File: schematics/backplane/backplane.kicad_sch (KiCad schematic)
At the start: 9 parts

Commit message: Update backplane, add power supply and debug port
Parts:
- removed MOD9: Module, cpu816footprints:BusSlot, symbol cpu816symbols:BusSlot
- added J1: Conn_01x02, Connector_BarrelJack:BarrelJack_SwitchcraftConxall_RAPC10U_Horizontal, symbol Connector_Generic:Conn_01x02
- added J2: Conn_01x20, Connector_PinSocket_2.54mm:PinSocket_1x20_P2.54mm_Vertical, symbol Connector_Generic:Conn_01x20
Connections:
- net DATA0: now also J2.13 (Pin_13)
- net DATA1: now also J2.14 (Pin_14)
- net DATA2: now also J2.15 (Pin_15)
- net DATA3: now also J2.16 (Pin_16)
- net DATA4: now also J2.17 (Pin_17)
- net DATA5: now also J2.18 (Pin_18)
- net DATA6: now also J2.19 (Pin_19)
- net DATA7: now also J2.20 (Pin_20)
- net GND: now also J1.2 (Pin_2), J2.1 (Pin_1), J2.2 (Pin_2)
- net PCINC: now also J2.4 (Pin_4)
- net STATE10: now also J2.7 (Pin_7)
- net STATE11: now also J2.8 (Pin_8)
- net STATE12: now also J2.9 (Pin_9)
- net STATE13: now also J2.10 (Pin_10)
- net STATE14: now also J2.11 (Pin_11)
- net STATE15: now also J2.12 (Pin_12)
- net STATE8: now also J2.5 (Pin_5)
- net STATE9: now also J2.6 (Pin_6)
- net VCC: now also J1.1 (Pin_1)
- net ~{SCCLR}: now also J2.3 (Pin_3)

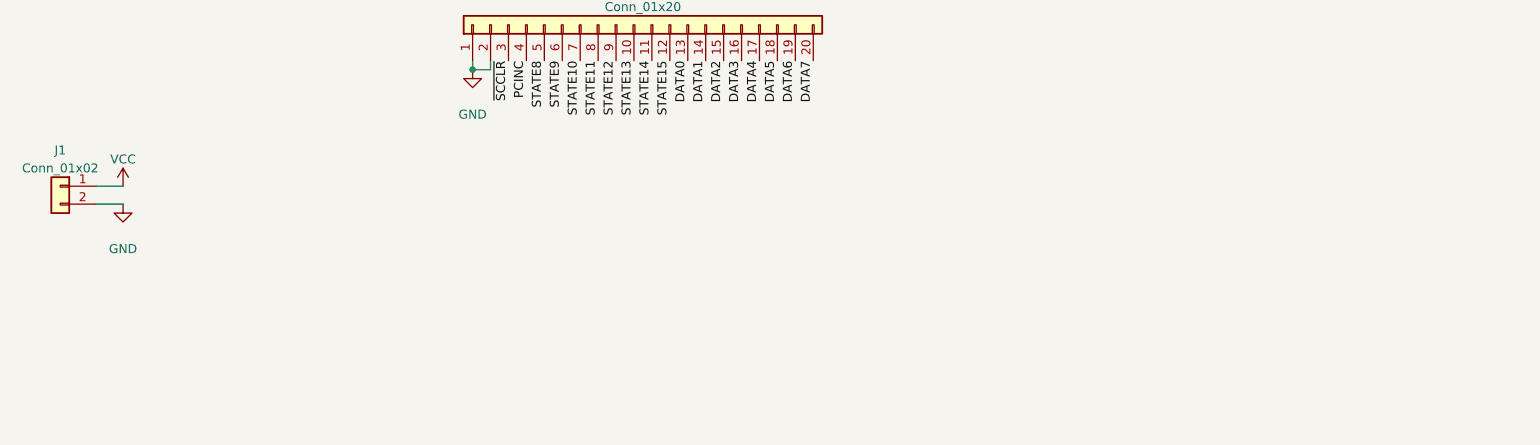
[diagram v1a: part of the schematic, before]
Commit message: fix(backplane): changed vcc and gnd connector
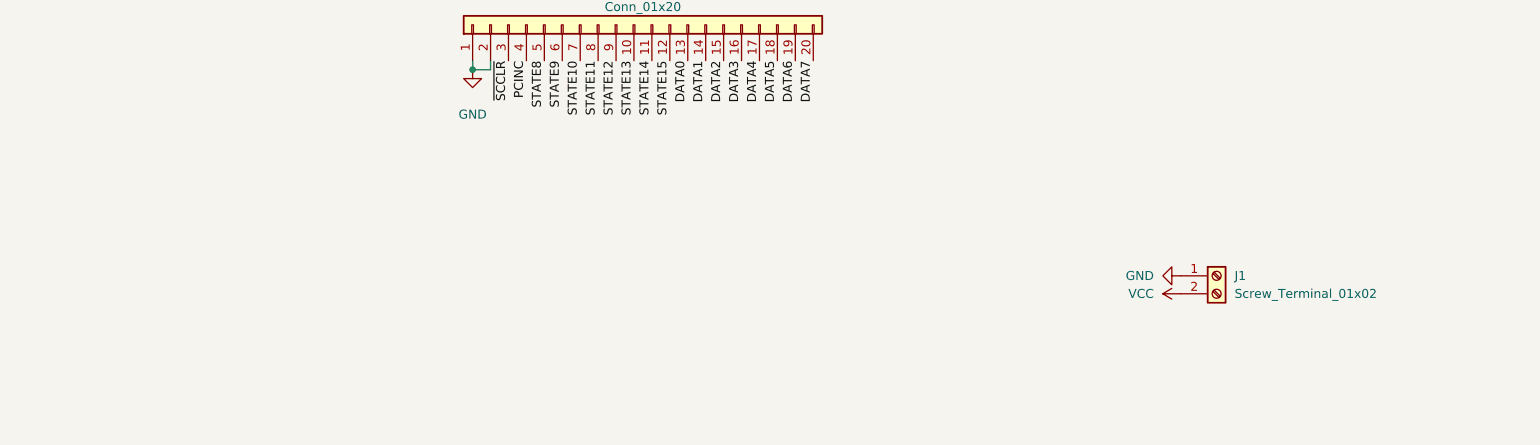
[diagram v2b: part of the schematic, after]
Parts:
- removed J1: Conn_01x02, Connector_BarrelJack:BarrelJack_SwitchcraftConxall_RAPC10U_Horizontal, symbol Connector_Generic:Conn_01x02
- added J1: Screw_Terminal_01x02, TerminalBlock_Phoenix:TerminalBlock_Phoenix_MKDS-1,5-2-5.08_1x02_P5.08mm_Horizontal, symbol Connector:Screw_Terminal_01x02
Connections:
- net GND: now also J1.1 (Pin_1)
- net VCC: now also J1.2 (Pin_2)
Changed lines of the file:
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@@
 	(wire
 		(pts
-			(xy -5.08 -12.7) (xy -8.89 -12.7)
-		)
-		(stroke
-			(width 0)
-			(type default)
-		)
-	)
-	(wire
-		(pts
-			(xy -5.08 -15.24) (xy -8.89 -15.24)
-		)
-		(stroke
-			(width 0)
-			(type default)
-		)
-	)
-	(wire
-		(pts
 			(xy 44.45 -33.02) (xy 44.45 -31.75)
 		)
@@
 	)
 	(symbol
-		(lib_id "power:VCC")
-		(at -5.08 -15.24 0)
-		(unit 1)
-		(exclude_from_sim no)
-		(in_bom yes)
-		(on_board yes)
-		(dnp no)
-		(property "Reference" "#PWR019"
-			(at -5.08 -11.43 0)
-			(effects
-				(font
-					(size 1.27 1.27)
-				)
-				(hide yes)
-			)
-		)
-		(property "Value" "VCC"
-			(at -5.08 -19.05 0)
-			(effects
-				(font
-					(size 1.27 1.27)
-				)
-			)
-		)
-		(property "Footprint" ""
-			(at -5.08 -15.24 0)
-			(effects
-				(font
-					(size 1.27 1.27)
-				)
-				(hide yes)
-			)
-		)
-		(property "Datasheet" ""
-			(at -5.08 -15.24 0)
-			(effects
-				(font
-					(size 1.27 1.27)
-				)
-				(hide yes)
-			)
-		)
-		(property "Description" "Power symbol creates a global label with name \"VCC\""
-			(at -5.08 -15.24 0)
-			(effects
-				(font
-					(size 1.27 1.27)
-				)
-				(hide yes)
-			)
-		)
-		(pin "1"
-		)
-		(instances
-			(project ""
-				(path "/805c276d-2b31-41a7-94f3-96d73c57e604"
-					(reference "#PWR019")
-					(unit 1)
-				)
-			)
-		)
-	)
-	(symbol
 		(lib_id "power:GND")
 		(at 466.09 165.1 0)
@@
 	)
 	(symbol
+		(lib_id "power:GND")
+		(at 144.78 -2.54 270)
+		(unit 1)
+		(exclude_from_sim no)
+		(in_bom yes)
+		(on_board yes)
+		(dnp no)
+		(fields_autoplaced yes)
+		(property "Reference" "#PWR019"
+			(at 138.43 -2.54 0)
+			(effects
+				(font
+					(size 1.27 1.27)
+				)
+				(hide yes)
+			)
+		)
+		(property "Value" "GND"
+			(at 140.97 -2.5401 90)
+			(effects
+				(font
+					(size 1.27 1.27)
+				)
+				(justify right)
+			)
+		)
+		(property "Footprint" ""
+			(at 144.78 -2.54 0)
+			(effects
+				(font
+					(size 1.27 1.27)
+				)
+				(hide yes)
+			)
+		)
+		(property "Datasheet" ""
+			(at 144.78 -2.54 0)
+			(effects
+				(font
+					(size 1.27 1.27)
+				)
+				(hide yes)
+			)
+		)
+		(property "Description" "Power symbol creates a global label with name \"GND\" , ground"
+			(at 144.78 -2.54 0)
+			(effects
+				(font
+					(size 1.27 1.27)
+				)
+				(hide yes)
+			)
+		)
+		(pin "1"
+		)
+		(instances
+			(project ""
+				(path "/805c276d-2b31-41a7-94f3-96d73c57e604"
+					(reference "#PWR019")
+					(unit 1)
+				)
+			)
+		)
+	)
+	(symbol
 		(lib_id "power:VCC")
 		(at 279.4 29.21 0)
@@
 	)
 	(symbol
-		(lib_id "power:GND")
-		(at -5.08 -12.7 0)
-		(unit 1)
-		(exclude_from_sim no)
-		(in_bom yes)
-		(on_board yes)
-		(dnp no)
-		(fields_autoplaced yes)
-		(property "Reference" "#PWR020"
-			(at -5.08 -6.35 0)
-			(effects
-				(font
-					(size 1.27 1.27)
-				)
-				(hide yes)
-			)
-		)
-		(property "Value" "GND"
-			(at -5.08 -6.35 0)
-			(effects
-				(font
-					(size 1.27 1.27)
-				)
-			)
-		)
-		(property "Footprint" ""
-			(at -5.08 -12.7 0)
-			(effects
-				(font
-					(size 1.27 1.27)
-				)
-				(hide yes)
-			)
-		)
-		(property "Datasheet" ""
-			(at -5.08 -12.7 0)
-			(effects
-				(font
-					(size 1.27 1.27)
-				)
-				(hide yes)
-			)
-		)
-		(property "Description" "Power symbol creates a global label with name \"GND\" , ground"
-			(at -5.08 -12.7 0)
-			(effects
-				(font
-					(size 1.27 1.27)
-				)
-				(hide yes)
-			)
-		)
-		(pin "1"
-		)
-		(instances
-			(project ""
-				(path "/805c276d-2b31-41a7-94f3-96d73c57e604"
-					(reference "#PWR020")
-					(unit 1)
-				)
-			)
-		)
-	)
-	(symbol
 		(lib_id "Connector_Generic:Conn_01x20")
 		(at 67.31 -38.1 90)
@@
 	)
 	(symbol
-		(lib_id "Connector_Generic:Conn_01x02")
-		(at -13.97 -15.24 0)
-		(mirror y)
-		(unit 1)
-		(exclude_from_sim no)
-		(in_bom yes)
-		(on_board yes)
-		(dnp no)
-		(fields_autoplaced yes)
-		(property "Reference" "J1"
-			(at -13.97 -20.32 0)
-			(effects
-				(font
-					(size 1.27 1.27)
-				)
-			)
-		)
-		(property "Value" "Conn_01x02"
-			(at -13.97 -17.78 0)
-			(effects
-				(font
-					(size 1.27 1.27)
-				)
-			)
-		)
-		(property "Footprint" "Connector_BarrelJack:BarrelJack_SwitchcraftConxall_RAPC10U_Horizontal"
-			(at -13.97 -15.24 0)
-			(effects
-				(font
-					(size 1.27 1.27)
-				)
-				(hide yes)
-			)
-		)
-		(property "Datasheet" "~"
-			(at -13.97 -15.24 0)
-			(effects
-				(font
-					(size 1.27 1.27)
-				)
-				(hide yes)
-			)
-		)
-		(property "Description" "Generic connector, single row, 01x02, script generated (kicad-library-utils/schlib/autogen/connector/)"
-			(at -13.97 -15.24 0)
-			(effects
-				(font
-					(size 1.27 1.27)
-				)
-				(hide yes)
-			)
-		)
-		(pin "2"
-		)
-		(pin "1"
-		)
-		(instances
-			(project ""
-				(path "/805c276d-2b31-41a7-94f3-96d73c57e604"
-					(reference "J1")
-					(unit 1)
-				)
-			)
-		)
-	)
-	(symbol
 		(lib_id "power:VCC")
 		(at 466.09 27.94 0)
@@
 	)
 	(symbol
+		(lib_id "Connector:Screw_Terminal_01x02")
+		(at 149.86 -2.54 0)
+		(unit 1)
+		(exclude_from_sim no)
+		(in_bom yes)
+		(on_board yes)
+		(dnp no)
+		(fields_autoplaced yes)
+		(property "Reference" "J1"
+			(at 152.4 -2.5401 0)
+			(effects
+				(font
+					(size 1.27 1.27)
+				)
+				(justify left)
+			)
+		)
+		(property "Value" "Screw_Terminal_01x02"
+			(at 152.4 -0.0001 0)
+			(effects
+				(font
+					(size 1.27 1.27)
+				)
+				(justify left)
+			)
+		)
+		(property "Footprint" "TerminalBlock_Phoenix:TerminalBlock_Phoenix_MKDS-1,5-2-5.08_1x02_P5.08mm_Horizontal"
+			(at 149.86 -2.54 0)
+			(effects
+				(font
+					(size 1.27 1.27)
+				)
+				(hide yes)
+			)
+		)
+		(property "Datasheet" "~"
+			(at 149.86 -2.54 0)
+			(effects
+				(font
+					(size 1.27 1.27)
+				)
+				(hide yes)
+			)
+		)
+		(property "Description" "Generic screw terminal, single row, 01x02, script generated (kicad-library-utils/schlib/autogen/connector/)"
+			(at 149.86 -2.54 0)
+			(effects
+				(font
+					(size 1.27 1.27)
+				)
+				(hide yes)
+			)
+		)
+		(pin "1"
+		)
+		(pin "2"
+		)
+		(instances
+			(project ""
+				(path "/805c276d-2b31-41a7-94f3-96d73c57e604"
+					(reference "J1")
+					(unit 1)
+				)
+			)
+		)
+	)
+	(symbol
 		(lib_id "power:GND")
 		(at 40.64 163.83 0)
@@
 					(unit 1)
 				)
+			)
+		)
+	)
+	(symbol
+		(lib_id "power:VCC")
+		(at 144.78 0 90)
+		(unit 1)
+		(exclude_from_sim no)
+		(in_bom yes)
+		(on_board yes)
+		(dnp no)
+		(fields_autoplaced yes)
+		(property "Reference" "#PWR017"
+			(at 148.59 0 0)
+			(effects
+				(font
+					(size 1.27 1.27)
+				)
+				(hide yes)
+			)
+		)
+		(property "Value" "VCC"
+			(at 140.97 -0.0001 90)
+			(effects
+				(font
+					(size 1.27 1.27)
+				)
+				(justify left)
+			)
+		)
+		(property "Footprint" ""
+			(at 144.78 0 0)
+			(effects
+				(font
+					(size 1.27 1.27)
+				)
+				(hide yes)
+			)
+		)
+		(property "Datasheet" ""
+			(at 144.78 0 0)
+			(effects
+				(font
+					(size 1.27 1.27)
+				)
+				(hide yes)
+			)
+		)
+		(property "Description" "Power symbol creates a global label with name \"VCC\""
+			(at 144.78 0 0)
+			(effects
+				(font
+					(size 1.27 1.27)
+				)
+				(hide yes)
+			)
+		)
+		(pin "1"
+		)
+		(instances
+			(project ""
+				(path "/805c276d-2b31-41a7-94f3-96d73c57e604"
+					(reference "#PWR017")
+					(unit 1)
+				)

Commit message: fix(backplane): removed duplicates of zones
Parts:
- J1: footprint TerminalBlock_Phoenix:TerminalBlock_Phoenix_MKDS-1,5-2-5.08_1x02_P5.08mm_Horizontal -> TerminalBlock_Degson:SHDR2W100P0X500_1X2_1000X780X1020P
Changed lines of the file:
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@@
 			)
 		)
-		(property "Footprint" "TerminalBlock_Phoenix:TerminalBlock_Phoenix_MKDS-1,5-2-5.08_1x02_P5.08mm_Horizontal"
+		(property "Footprint" "TerminalBlock_Degson:SHDR2W100P0X500_1X2_1000X780X1020P"
 			(at 149.86 -2.54 0)
 			(effects

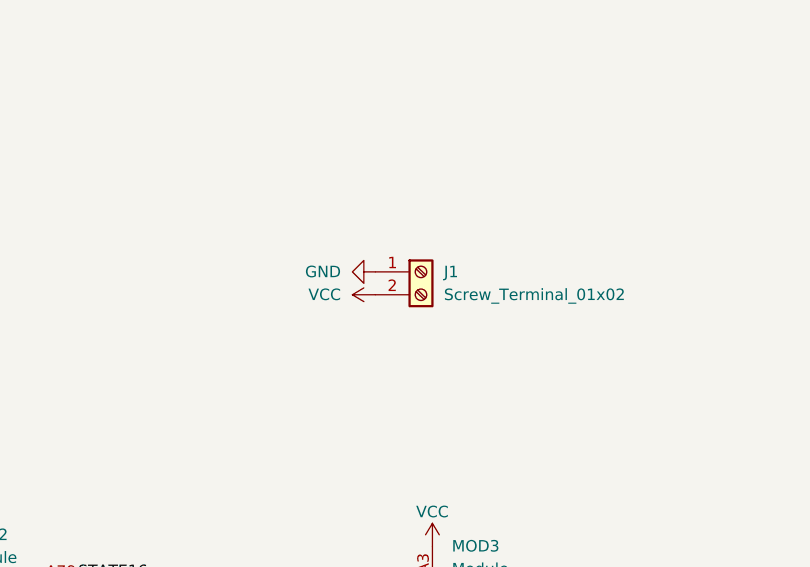
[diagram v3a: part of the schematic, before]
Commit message: Add test points
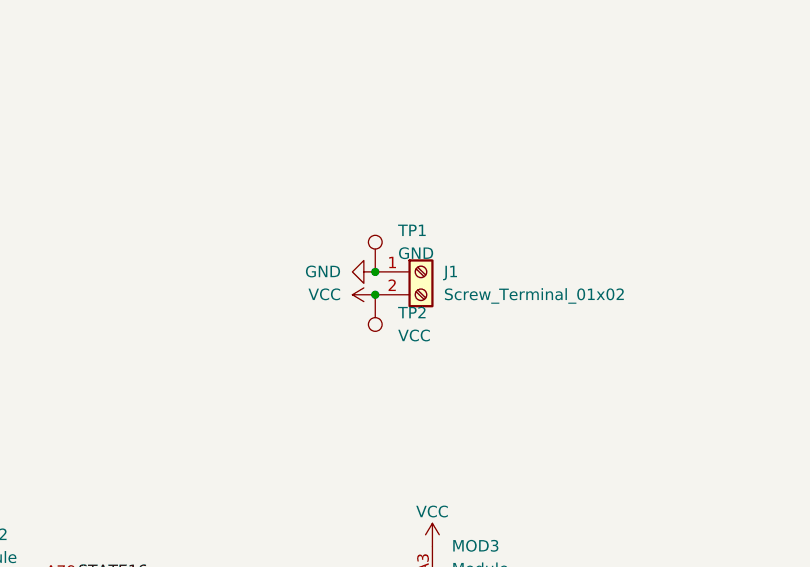
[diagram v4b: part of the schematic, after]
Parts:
- added TP1: GND, TestPoint:TestPoint_Pad_D1.5mm, symbol Connector:TestPoint
- added TP2: VCC, TestPoint:TestPoint_Pad_D1.5mm, symbol Connector:TestPoint
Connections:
- net GND: now also TP1.1
- net VCC: now also TP2.1
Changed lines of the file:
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@@
 		(color 0 0 0 0)
 	)
+	(junction
+		(at 144.78 -2.54)
+		(diameter 0)
+		(color 0 0 0 0)
+	)
+	(junction
+		(at 144.78 0)
+		(diameter 0)
+		(color 0 0 0 0)
+	)
 	(wire
 		(pts
@@
 	)
 	(symbol
+		(lib_id "Connector:TestPoint")
+		(at 144.78 0 180)
+		(unit 1)
+		(exclude_from_sim no)
+		(in_bom yes)
+		(on_board yes)
+		(dnp no)
+		(fields_autoplaced yes)
+		(property "Reference" "TP2"
+			(at 147.32 2.0319 0)
+			(effects
+				(font
+					(size 1.27 1.27)
+				)
+				(justify right)
+			)
+		)
+		(property "Value" "VCC"
+			(at 147.32 4.5719 0)
+			(effects
+				(font
+					(size 1.27 1.27)
+				)
+				(justify right)
+			)
+		)
+		(property "Footprint" "TestPoint:TestPoint_Pad_D1.5mm"
+			(at 139.7 0 0)
+			(effects
+				(font
+					(size 1.27 1.27)
+				)
+				(hide yes)
+			)
+		)
+		(property "Datasheet" "~"
+			(at 139.7 0 0)
+			(effects
+				(font
+					(size 1.27 1.27)
+				)
+				(hide yes)
+			)
+		)
+		(property "Description" "test point"
+			(at 144.78 0 0)
+			(effects
+				(font
+					(size 1.27 1.27)
+				)
+				(hide yes)
+			)
+		)
+		(pin "1"
+		)
+		(instances
+			(project "backplane"
+				(path "/805c276d-2b31-41a7-94f3-96d73c57e604"
+					(reference "TP2")
+					(unit 1)
+				)
+			)
+		)
+	)
+	(symbol
 		(lib_id "cpu816symbols:BusSlot")
 		(at 40.64 95.25 0)
@@
 					(unit 1)
 				)
+			)
+		)
+	)
+	(symbol
+		(lib_id "Connector:TestPoint")
+		(at 144.78 -2.54 0)
+		(unit 1)
+		(exclude_from_sim no)
+		(in_bom yes)
+		(on_board yes)
+		(dnp no)
+		(fields_autoplaced yes)
+		(property "Reference" "TP1"
+			(at 147.32 -7.1121 0)
+			(effects
+				(font
+					(size 1.27 1.27)
+				)
+				(justify left)
+			)
+		)
+		(property "Value" "GND"
+			(at 147.32 -4.5721 0)
+			(effects
+				(font
+					(size 1.27 1.27)
+				)
+				(justify left)
+			)
+		)
+		(property "Footprint" "TestPoint:TestPoint_Pad_D1.5mm"
+			(at 149.86 -2.54 0)
+			(effects
+				(font
+					(size 1.27 1.27)
+				)
+				(hide yes)
+			)
+		)
+		(property "Datasheet" "~"
+			(at 149.86 -2.54 0)
+			(effects
+				(font
+					(size 1.27 1.27)
+				)
+				(hide yes)
+			)
+		)
+		(property "Description" "test point"
+			(at 144.78 -2.54 0)
+			(effects
+				(font
+					(size 1.27 1.27)
+				)
+				(hide yes)
+			)
+		)
+		(pin "1"
+		)
+		(instances
+			(project ""
+				(path "/805c276d-2b31-41a7-94f3-96d73c57e604"
+					(reference "TP1")
+					(unit 1)
+				)
